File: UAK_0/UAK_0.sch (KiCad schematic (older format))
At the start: 54 parts, among them K1 Кнопка_FSMSM, K2 Кнопка_FSMSM, X1 Крепежное_отверстие_М3, X2 Крепежное_отверстие_М3, X3 Крепежное_отверстие_М3, X4 Крепежное_отверстие_М3

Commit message: подготовлена схема UAK_0A
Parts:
- DA1: renamed from DA?; footprint (none) -> N_DD:DIP6
- gave numbers to parts that had none: 8
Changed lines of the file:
@@
 СДВОЕННЫЙ
 $Comp
-L elements:Предохранитель FU?
+L elements:Предохранитель FU2
 U 1 1 5F560616
 P 5350 5600
-AR Path="/5F560616" Ref="FU?"  Part="1"
+AR Path="/5F560616" Ref="FU2"  Part="1"
 AR Path="/5F540B17/5F560616" Ref="FU?"  Part="1"
-F 0 "FU?" H 5350 5750 60  0000 C CNN
+F 0 "FU2" H 5350 5750 60  0000 C CNN
 F 1 "Предохранитель" H 5350 5450 60  0001 C CNN
 F 2 "N_RLC:Предохранитель_SMD_1812" H 5350 5600 60  0001 C CNN
@@
 $EndComp
 $Comp
-L elements_2020:Клеммник_х2_KLS2-300-5.00-02P-2S XT?
+L elements_2020:Клеммник_х2_KLS2-300-5.00-02P-2S XT8
 U 1 1 5F5696D9
 P 5750 7000
-F 0 "XT?" H 5400 7350 60  0000 L CNN
+F 0 "XT8" H 5400 7350 60  0000 L CNN
 F 1 "Клеммник_х2_KLS2-300-5.00-02P-2S" H 5440 6740 60  0001 C CNN
 F 2 "N_X:Клеммник_х2_шаг5" H 5175 7275 60  0001 C CNN
@@
 220_L
 $Comp
-L elements_2020:МОП-реле_КР293КП1Б DA?
+L elements_2020:МОП-реле_КР293КП1Б DA1
 U 1 1 5F56E7B1
 P 4100 5900
-F 0 "DA?" H 4350 5500 50  0000 C CNN
+F 0 "DA1" H 4350 5500 50  0000 C CNN
 F 1 "МОП-реле_КР293КП1Б" H 4000 6150 50  0001 C CNN
-F 2 "" H 4100 5900 50  0001 C CNN
+F 2 "N_DD:DIP6" H 4100 5900 50  0001 C CNN
 F 3 "" H 4100 5900 50  0001 C CNN
 F 4 "КР293КП1Б/АОУ163А" H 4350 6000 50  0000 C CNN "INFO"
@@
 P 3400 5750
 AR Path="/5F540B17/5F5B8E8E" Ref="R?"  Part="1"
-AR Path="/5F5B8E8E" Ref="R?"  Part="1"
-F 0 "R?" H 3350 5900 60  0000 L CNN
+AR Path="/5F5B8E8E" Ref="R21"  Part="1"
+F 0 "R21" H 3350 5900 60  0000 L CNN
 F 1 "Резистор_0,065Вт" H 3400 5600 60  0001 C CNN
 F 2 "N_RLC:Резистор_SMD_0603_0,065_Вт" H 3400 5750 60  0001 C CNN
@@
 P 3050 7150
 AR Path="/5F540B17/5F5D0ED9" Ref="R?"  Part="1"
-AR Path="/5F5D0ED9" Ref="R?"  Part="1"
-F 0 "R?" H 3000 7000 60  0000 L CNN
+AR Path="/5F5D0ED9" Ref="R20"  Part="1"
+F 0 "R20" H 3000 7000 60  0000 L CNN
 F 1 "Резистор_0,065Вт" H 3050 7000 60  0001 C CNN
 F 2 "N_RLC:Резистор_SMD_0603_0,065_Вт" H 3050 7150 60  0001 C CNN
@@
 P 1950 6650
 AR Path="/5F540B17/5F5D0EE5" Ref="R?"  Part="1"
-AR Path="/5F5D0EE5" Ref="R?"  Part="1"
-F 0 "R?" H 1900 6800 60  0000 L CNN
+AR Path="/5F5D0EE5" Ref="R19"  Part="1"
+F 0 "R19" H 1900 6800 60  0000 L CNN
 F 1 "Резистор_0,065Вт" H 1950 6500 60  0001 C CNN
 F 2 "N_RLC:Резистор_SMD_0603_0,065_Вт" H 1950 6650 60  0001 C CNN
@@
 $EndComp
 $Comp
-L elements_2020:Транзистор_полевой_N-канальный_IRLML6344TR VT?
+L elements_2020:Транзистор_полевой_N-канальный_IRLML6344TR VT4
 U 1 1 5F5D0EF1
 P 3000 6650
-F 0 "VT?" H 3350 7150 60  0000 C CNN
+F 0 "VT4" H 3350 7150 60  0000 C CNN
 F 1 "Транзистор_полевой_N-канальный_IRLML6344TR" H 3200 6400 60  0001 C CNN
 F 2 "MOTOR_VD_VT_HL:Корпус_КТ-46" H 3075 7325 60  0001 C CNN
@@
 	1000 2350 1500 2350
 $Comp
-L elements:Резистор_0,25Вт R?
+L elements:Резистор_0,25Вт R22
 U 1 1 5F6B16D8
 P 4750 6800
-F 0 "R?" V 4705 6903 60  0000 L CNN
+F 0 "R22" V 4705 6903 60  0000 L CNN
 F 1 "Резистор_0,25Вт" H 4750 6650 60  0001 C CNN
 F 2 "N_RLC:Резистор_SMD_1206-0,25_Вт" H 4750 6800 60  0001 C CNN
@@
 КОММУТАЦИЯ 220В
 $Comp
-L elements:Конденсатор_керамический C?
+L elements:Конденсатор_керамический C17
 U 1 1 5F6EF61F
 P 4750 7400
-AR Path="/5F6EF61F" Ref="C?"  Part="1"
+AR Path="/5F6EF61F" Ref="C17"  Part="1"
 AR Path="/5F540B17/5F6EF61F" Ref="C?"  Part="1"
-F 0 "C?" V 4730 7488 60  0000 L CNN
+F 0 "C17" V 4730 7488 60  0000 L CNN
 F 1 "Конденсатор_керамический" H 4850 7300 60  0001 C CNN
 F 2 "N_RLC:Конденсатор_SMD_1210" H 4750 7400 60  0001 C CNN

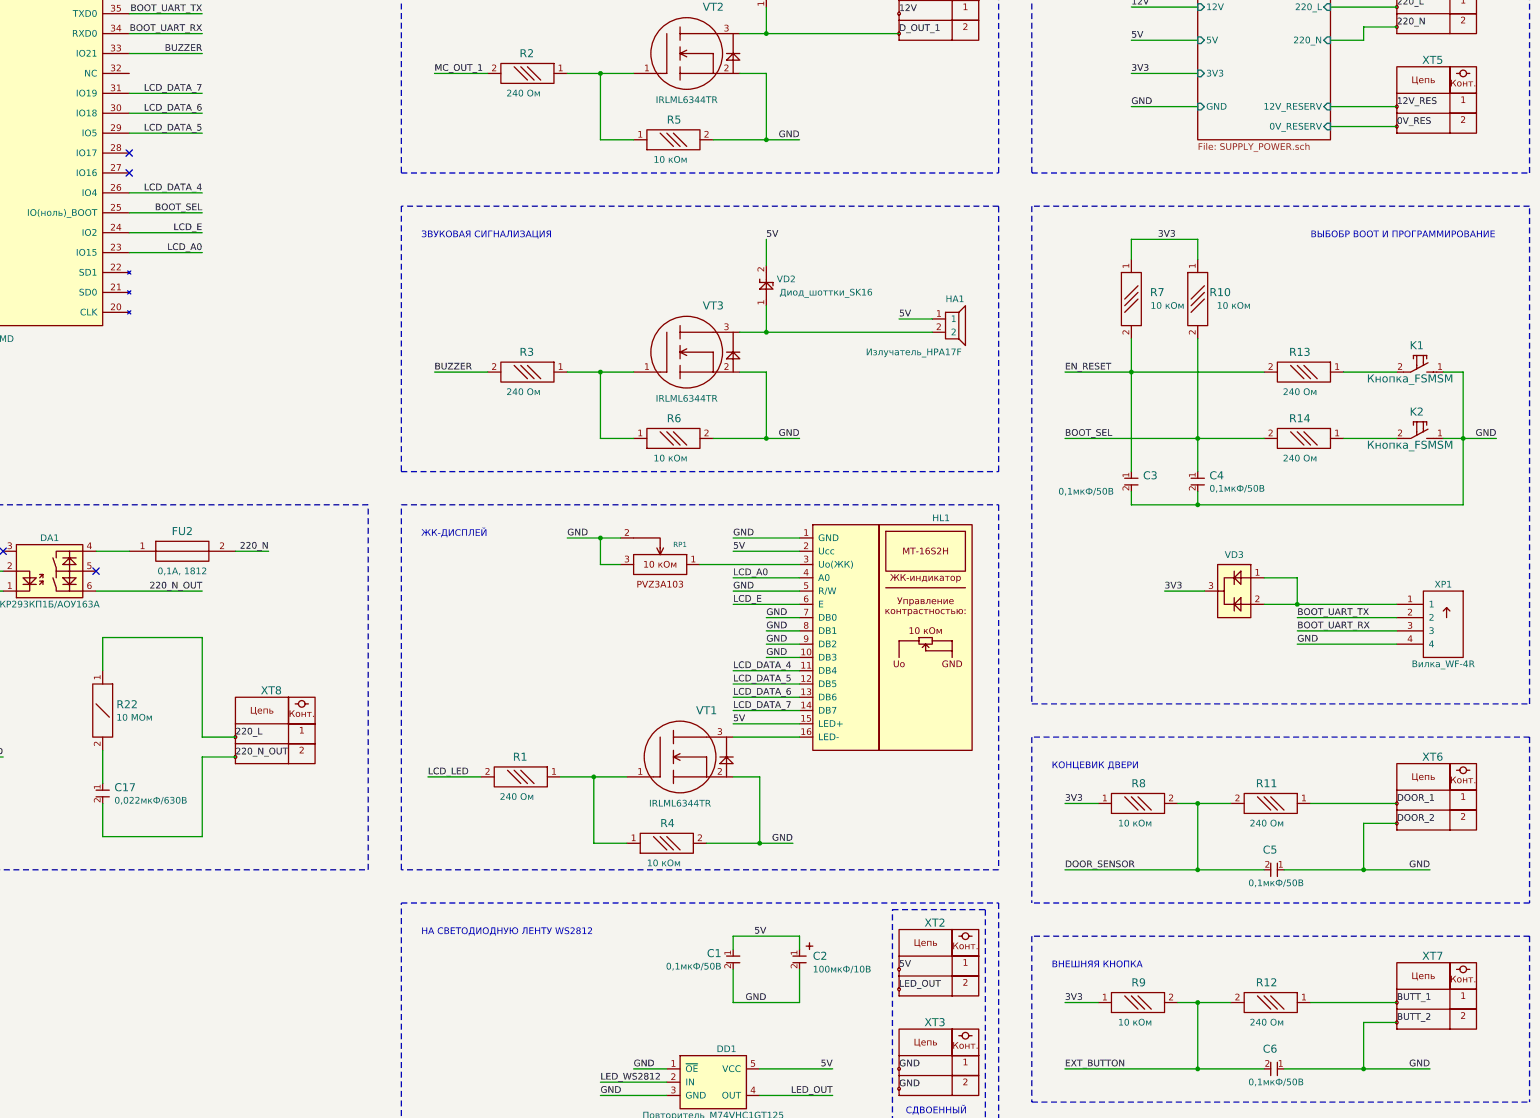
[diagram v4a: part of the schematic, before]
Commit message: есть трассировка питания
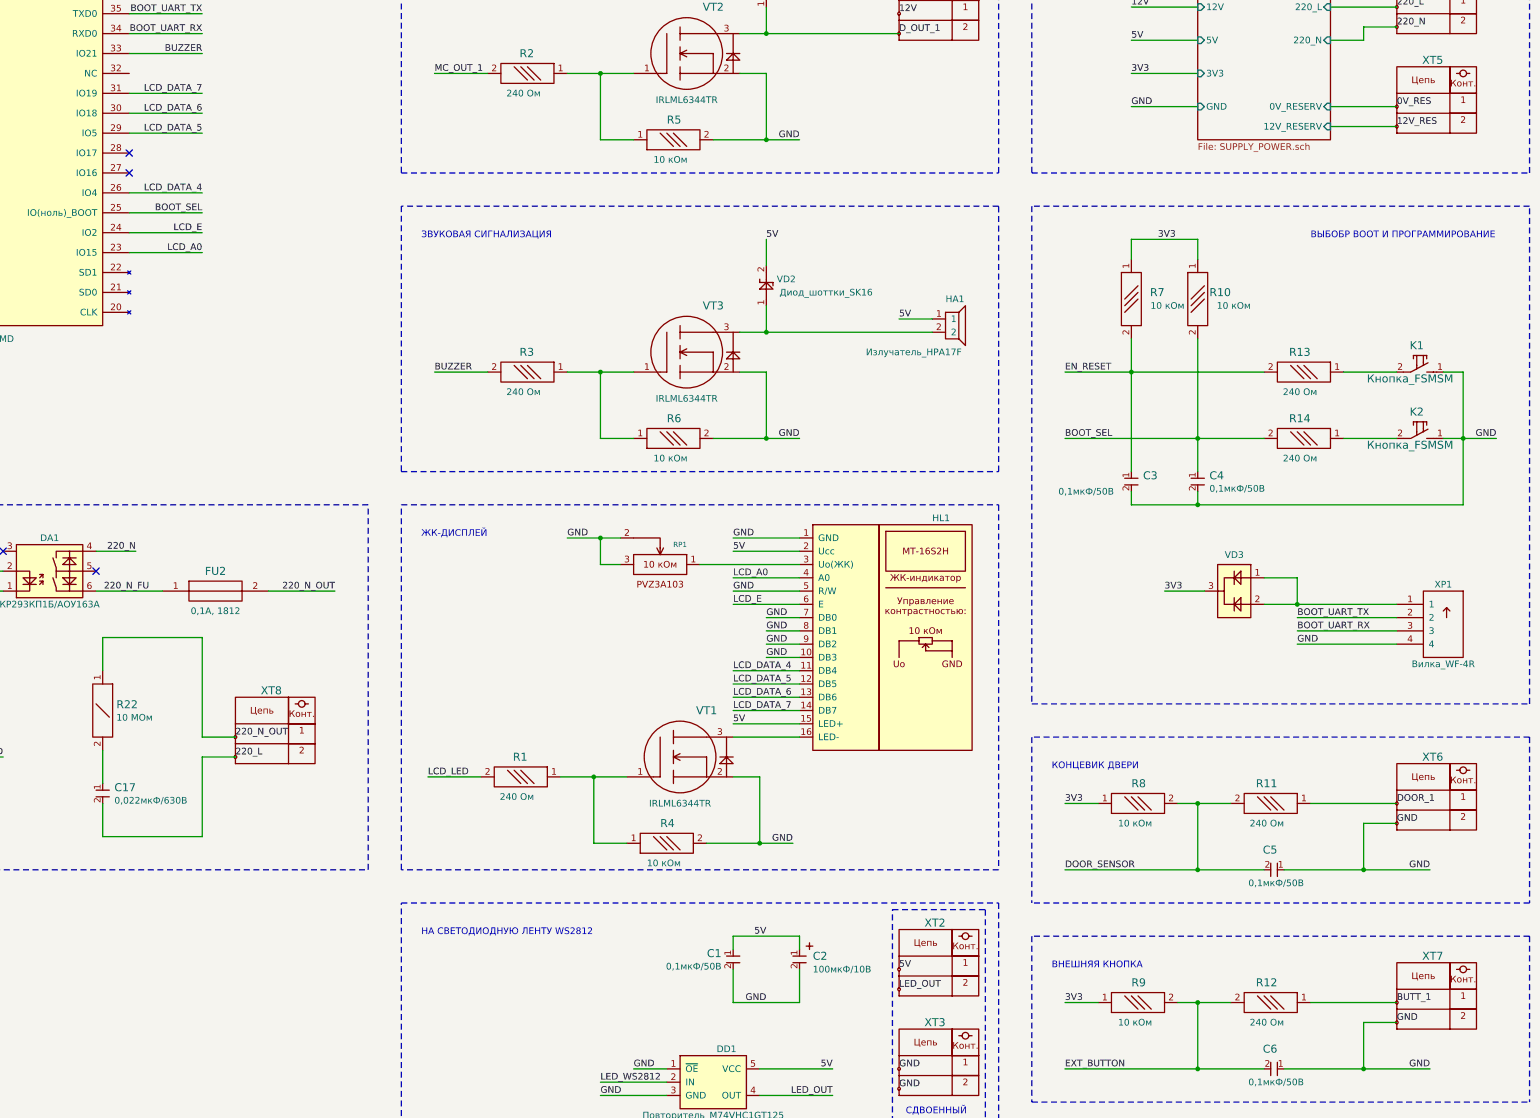
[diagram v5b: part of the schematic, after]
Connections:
- net 0V_RES: now also XT5.1; no longer XT5.2
- net 12V_RES: now also XT5.2; no longer XT5.1
- net 220_L: now also C17.2, XT8.2; no longer R22.1, XT8.1
- net 220_N: now also DA1.4; no longer FU2.2
- net 220_N_OUT: now also FU2.2, R22.1, XT8.1; no longer C17.2, DA1.6, XT8.2
- net 220_N_FU: now reaches FU2.1
- net 220_N_FU: now also DA1.6; no longer DA1.4
- net BUTT_2 renamed GND
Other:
- moved on the sheet: FU2
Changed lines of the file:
@@
 F6 "5V" I L 13000 1750 50
 F7 "12V" I L 13000 1500 50
-F8 "12V_RESERV" I R 14000 2250 50
-F9 "0V_RESERV" I R 14000 2400 50
+F8 "12V_RESERV" I R 14000 2400 50
+F9 "0V_RESERV" I R 14000 2250 50
 $EndSheet
 Wire Wire Line
@@
 Text Label 14500 7500 0    50   ~ 0
 DOOR_1
-Text Label 14500 7650 0    50   ~ 0
-DOOR_2
 Wire Notes Line
 	15500 7000 11750 7000
@@
 Text Label 14500 9000 0    50   ~ 0
 BUTT_1
-Text Label 14500 9150 0    50   ~ 0
-BUTT_2
 Wire Notes Line
 	11750 9750 15500 9750
@@
 Wire Wire Line
 	14000 2400 14500 2400
+Text Label 14500 2400 0    50   ~ 0
+12V_RES
 Text Label 14500 2250 0    50   ~ 0
-12V_RES
-Text Label 14500 2400 0    50   ~ 0
 0V_RES
 Wire Notes Line
@@
 L elements:Предохранитель FU2
 U 1 1 5F560616
-P 5350 5600
+P 5600 5900
 AR Path="/5F560616" Ref="FU2"  Part="1"
 AR Path="/5F540B17/5F560616" Ref="FU?"  Part="1"
-F 0 "FU2" H 5350 5750 60  0000 C CNN
-F 1 "Предохранитель" H 5350 5450 60  0001 C CNN
-F 2 "N_RLC:Предохранитель_SMD_1812" H 5350 5600 60  0001 C CNN
-F 3 "" H 5350 5600 60  0001 C CNN
-F 4 "0,1А, 1812" H 5350 5450 50  0000 C CNN "INFO"
-F 5 "https://www.chipdip.ru/product/mf-msmf010" H 5350 5600 50  0001 C CNN "LINK"
-	1    5350 5600
+F 0 "FU2" H 5600 6050 60  0000 C CNN
+F 1 "Предохранитель" H 5600 5750 60  0001 C CNN
+F 2 "N_RLC:Предохранитель_SMD_1812" H 5600 5900 60  0001 C CNN
+F 3 "" H 5600 5900 60  0001 C CNN
+F 4 "0,1А, 1812" H 5600 5750 50  0000 C CNN "INFO"
+F 5 "https://www.chipdip.ru/product/mf-msmf010" H 5600 5900 50  0001 C CNN "LINK"
+	1    5600 5900
 	1    0    0    -1
 $EndComp
@@
 	-1   0    0    -1
 $EndComp
-Text Label 5750 7000 0    50   ~ 0
+Text Label 5750 7150 0    50   ~ 0
 220_L
 $Comp
@@
 	1    0    0    1
 $EndComp
-Text Label 6000 5600 2    50   ~ 0
+Text Label 5000 5600 2    50   ~ 0
 220_N
-Wire Wire Line
-	6000 5600 5750 5600
 NoConn ~ 4700 5750
 NoConn ~ 4000 5600
-Wire Wire Line
-	4700 5900 5500 5900
-Text Label 5500 5900 2    50   ~ 0
+Text Label 6500 5900 2    50   ~ 0
 220_N_OUT
-Text Label 5750 7150 0    50   ~ 0
+Text Label 5750 7000 0    50   ~ 0
 220_N_OUT
 $Comp
@@
 Wire Wire Line
 	3750 5900 3750 6350
-Wire Wire Line
-	4700 5600 4950 5600
 Text Label 1000 2350 0    50   ~ 0
 MC_220_OUT
@@
 Text Label 2950 5750 0    50   ~ 0
 3V3
+Wire Wire Line
+	4700 5600 5000 5600
+Wire Wire Line
+	6000 5900 6500 5900
+Text Label 5100 5900 2    50   ~ 0
+220_N_FU
+Wire Wire Line
+	4700 5900 5200 5900
+Text Label 14500 7650 0    50   ~ 0
+GND
+Text Label 14500 9150 0    50   ~ 0
+GND
 $EndSCHEMATC

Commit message: начата установка ESP32
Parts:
- C2: symbol MOTOR_2020_components:Конденсатор_К53-56А-32В-22_мкФ+-10проц. -> UAK_0-rescue:Конденсатор_К53-56А-32В-22_мкФ+-10проц.-MOTOR_2020_components
- DA1: symbol elements_2020:МОП-реле_КР293КП1Б -> UAK_0-rescue:МОП-реле_КР293КП1Б-elements_2020
- DD1: symbol elements_2020:Повторитель_M74VHC1GT125 -> UAK_0-rescue:Повторитель_M74VHC1GT125-elements_2020
- HA1: symbol elements_2020:Излучатель_HPA17F -> UAK_0-rescue:Излучатель_HPA17F-elements_2020
- HL1: symbol elements_2020:Жидкокристалический_индикатор_MT-16S2H-2KLW -> UAK_0-rescue:Жидкокристалический_индикатор_MT-16S2H-2KLW-elements_2020
- RP1: symbol elements_2020:Резистор_подстроечный_PVA3A103 -> UAK_0-rescue:Резистор_подстроечный_PVA3A103-elements_2020
- VD1, VD2: symbol elements_2020:Диод_шоттки_SK16 -> UAK_0-rescue:Диод_шоттки_SK16-elements_2020
- VD3: symbol MOTOR_2020_components:Набор_диодов_2Д803АС9 -> UAK_0-rescue:Набор_диодов_2Д803АС9-MOTOR_2020_components
- VT1, VT2, VT3, VT4: symbol elements_2020:Транзистор_полевой_N-канальный_IRLML6344TR -> UAK_0-rescue:Транзистор_полевой_N-канальный_IRLML6344TR-elements_2020
- X1, X2, X3, X4: symbol MOTOR_2020_components:Крепежное_отверстие_М3 -> UAK_0-rescue:Крепежное_отверстие_М3-MOTOR_2020_components
- XP1: symbol MOTOR_2020_components:Вилка_СНП389-4ВП32-1-1 -> UAK_0-rescue:Вилка_СНП389-4ВП32-1-1-MOTOR_2020_components
- XT1, XT2, XT3, XT4, XT5, XT6, XT7, XT8: symbol elements_2020:Клеммник_х2_KLS2-300-5.00-02P-2S -> UAK_0-rescue:Клеммник_х2_KLS2-300-5.00-02P-2S-elements_2020
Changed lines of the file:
@@
 EESchema Schematic File Version 4
 LIBS:UAK_0-cache
-EELAYER 30 0
+EELAYER 29 0
 EELAYER END
 $Descr A3 16535 11693
@@
 $EndComp
 $Comp
-L elements_2020:Клеммник_х2_KLS2-300-5.00-02P-2S XT4
+L UAK_0-rescue:Клеммник_х2_KLS2-300-5.00-02P-2S-elements_2020 XT4
 U 1 1 5F53E542
 P 14500 1500
@@
 	14500 4750 14100 4750
 $Comp
-L MOTOR_2020_components:Набор_диодов_2Д803АС9 VD3
+L UAK_0-rescue:Набор_диодов_2Д803АС9-MOTOR_2020_components VD3
 U 1 1 5F55ECC5
 P 13500 5800
@@
 BOOT_UART_RX
 $Comp
-L MOTOR_2020_components:Вилка_СНП389-4ВП32-1-1 XP1
+L UAK_0-rescue:Вилка_СНП389-4ВП32-1-1-MOTOR_2020_components XP1
 U 1 1 5F5606D4
 P 15000 5900
@@
 	13000 8000 13000 7500
 $Comp
-L elements_2020:Клеммник_х2_KLS2-300-5.00-02P-2S XT6
+L UAK_0-rescue:Клеммник_х2_KLS2-300-5.00-02P-2S-elements_2020 XT6
 U 1 1 5F598429
 P 14500 7500
@@
 КОНЦЕВИК ДВЕРИ
 $Comp
-L elements_2020:Транзистор_полевой_N-канальный_IRLML6344TR VT2
+L UAK_0-rescue:Транзистор_полевой_N-канальный_IRLML6344TR-elements_2020 VT2
 U 1 1 5F5AB6F0
 P 9000 2000
@@
 GND
 $Comp
-L elements_2020:Клеммник_х2_KLS2-300-5.00-02P-2S XT1
+L UAK_0-rescue:Клеммник_х2_KLS2-300-5.00-02P-2S-elements_2020 XT1
 U 1 1 5F5B9CF4
 P 10750 1550
@@
 12V
 $Comp
-L elements_2020:Диод_шоттки_SK16 VD1
+L UAK_0-rescue:Диод_шоттки_SK16-elements_2020 VD1
 U 1 1 5F5C4406
 P 9750 1500
@@
 	4950 2150 5500 2150
 $Comp
-L MOTOR_2020_components:Крепежное_отверстие_М3 X4
+L UAK_0-rescue:Крепежное_отверстие_М3-MOTOR_2020_components X4
 U 1 1 5F5D023C
 P 11000 10500
@@
 $EndComp
 $Comp
-L MOTOR_2020_components:Крепежное_отверстие_М3 X3
+L UAK_0-rescue:Крепежное_отверстие_М3-MOTOR_2020_components X3
 U 1 1 5F5D0231
 P 10500 10500
@@
 $EndComp
 $Comp
-L MOTOR_2020_components:Крепежное_отверстие_М3 X2
+L UAK_0-rescue:Крепежное_отверстие_М3-MOTOR_2020_components X2
 U 1 1 5F5CFEAE
 P 10000 10500
@@
 $EndComp
 $Comp
-L MOTOR_2020_components:Крепежное_отверстие_М3 X1
+L UAK_0-rescue:Крепежное_отверстие_М3-MOTOR_2020_components X1
 U 1 1 5F5CFB44
 P 9500 10500
@@
 	10000 5700 9250 5700
 $Comp
-L elements_2020:Резистор_подстроечный_PVA3A103 RP1
+L UAK_0-rescue:Резистор_подстроечный_PVA3A103-elements_2020 RP1
 U 1 1 5F651E48
 P 9300 5100
@@
 $EndComp
 $Comp
-L elements_2020:Транзистор_полевой_N-канальный_IRLML6344TR VT1
+L UAK_0-rescue:Транзистор_полевой_N-канальный_IRLML6344TR-elements_2020 VT1
 U 1 1 5F61B72E
 P 8950 7300
@@
 	9750 3950 11000 3950
 $Comp
-L elements_2020:Излучатель_HPA17F HA1
+L UAK_0-rescue:Излучатель_HPA17F-elements_2020 HA1
 U 1 1 5F5EFC61
 P 11100 3850
@@
 	9550 3950 9750 3950
 $Comp
-L elements_2020:Диод_шоттки_SK16 VD2
+L UAK_0-rescue:Диод_шоттки_SK16-elements_2020 VD2
 U 1 1 5F5E6E89
 P 9750 3750
@@
 $EndComp
 $Comp
-L elements_2020:Транзистор_полевой_N-канальный_IRLML6344TR VT3
+L UAK_0-rescue:Транзистор_полевой_N-канальный_IRLML6344TR-elements_2020 VT3
 U 1 1 5F5E6E4B
 P 9000 4250
@@
 $EndComp
 $Comp
-L elements_2020:Жидкокристалический_индикатор_MT-16S2H-2KLW HL1
+L UAK_0-rescue:Жидкокристалический_индикатор_MT-16S2H-2KLW-elements_2020 HL1
 U 1 1 5F5D943F
 P 10000 5500
@@
 	13000 9500 13000 9000
 $Comp
-L elements_2020:Клеммник_х2_KLS2-300-5.00-02P-2S XT7
+L UAK_0-rescue:Клеммник_х2_KLS2-300-5.00-02P-2S-elements_2020 XT7
 U 1 1 5F5BFDD6
 P 14500 9000
@@
 NoConn ~ 1500 3400
 $Comp
-L elements_2020:Повторитель_M74VHC1GT125 DD1
+L UAK_0-rescue:Повторитель_M74VHC1GT125-elements_2020 DD1
 U 1 1 5F73F35E
 P 9100 9500
@@
 5V
 $Comp
-L MOTOR_2020_components:Конденсатор_К53-56А-32В-22_мкФ+-10проц. C2
+L UAK_0-rescue:Конденсатор_К53-56А-32В-22_мкФ+-10проц.-MOTOR_2020_components C2
 U 1 1 5F75AF76
 P 10000 8650
@@
 	4950 1400 5500 1400
 $Comp
-L elements_2020:Клеммник_х2_KLS2-300-5.00-02P-2S XT2
+L UAK_0-rescue:Клеммник_х2_KLS2-300-5.00-02P-2S-elements_2020 XT2
 U 1 1 5F79F40F
 P 10750 8750
@@
 $EndComp
 $Comp
-L elements_2020:Клеммник_х2_KLS2-300-5.00-02P-2S XT3
+L UAK_0-rescue:Клеммник_х2_KLS2-300-5.00-02P-2S-elements_2020 XT3
 U 1 1 5F7A0B62
 P 10750 9500
@@
 НА СВЕТОДИОДНУЮ ЛЕНТУ WS2812
 $Comp
-L elements_2020:Клеммник_х2_KLS2-300-5.00-02P-2S XT5
+L UAK_0-rescue:Клеммник_х2_KLS2-300-5.00-02P-2S-elements_2020 XT5
 U 1 1 5F82F0A6
 P 14500 2250
@@
 $EndComp
 $Comp
-L elements_2020:Клеммник_х2_KLS2-300-5.00-02P-2S XT8
+L UAK_0-rescue:Клеммник_х2_KLS2-300-5.00-02P-2S-elements_2020 XT8
 U 1 1 5F5696D9
 P 5750 7000
@@
 220_L
 $Comp
-L elements_2020:МОП-реле_КР293КП1Б DA1
+L UAK_0-rescue:МОП-реле_КР293КП1Б-elements_2020 DA1
 U 1 1 5F56E7B1
 P 4100 5900
@@
 $EndComp
 $Comp
-L elements_2020:Транзистор_полевой_N-канальный_IRLML6344TR VT4
+L UAK_0-rescue:Транзистор_полевой_N-канальный_IRLML6344TR-elements_2020 VT4
 U 1 1 5F5D0EF1
 P 3000 6650

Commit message: закончена трассировка, обновлена PDF и PNG, добавлен STEP
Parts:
- added D1: NI, N_ICO:ni_10x10, symbol elements:LOGO
- added D2: QR, N_ICO:El-nikitos_QR_10x10, symbol elements:LOGO
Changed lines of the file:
@@
 EESchema Schematic File Version 4
 LIBS:UAK_0-cache
-EELAYER 29 0
+EELAYER 30 0
 EELAYER END
 $Descr A3 16535 11693
 encoding utf-8
 Sheet 1 2
-Title ""
+Title "UAK.0B.M9"
 Date ""
 Rev ""
@@
 Text Label 14500 9150 0    50   ~ 0
 GND
+$Comp
+L elements:LOGO D1
+U 1 1 5F67ECD6
+P 8500 10500
+F 0 "D1" H 8425 10700 50  0001 C CNN
+F 1 "NI" H 8450 10500 50  0000 L CNN
+F 2 "N_ICO:ni_10x10" H 8500 10500 50  0001 C CNN
+F 3 "" H 8500 10500 50  0001 C CNN
+	1    8500 10500
+	1    0    0    -1
+$EndComp
+$Comp
+L elements:LOGO D2
+U 1 1 5F67F5F9
+P 9000 10500
+F 0 "D2" H 8925 10700 50  0001 C CNN
+F 1 "QR" H 8950 10500 50  0000 L CNN
+F 2 "N_ICO:El-nikitos_QR_10x10" H 9000 10500 50  0001 C CNN
+F 3 "" H 9000 10500 50  0001 C CNN
+	1    9000 10500
+	1    0    0    -1
+$EndComp
 $EndSCHEMATC

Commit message: UAK_0C. Убрал лого Ni, добавлены gerber
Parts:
- removed D1: NI, N_ICO:ni_10x10, symbol elements:LOGO
- removed D2: QR, N_ICO:El-nikitos_QR_10x10, symbol elements:LOGO
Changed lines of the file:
@@
 EESchema Schematic File Version 4
 LIBS:UAK_0-cache
-EELAYER 30 0
+EELAYER 29 0
 EELAYER END
 $Descr A3 16535 11693
 encoding utf-8
 Sheet 1 2
-Title "UAK.0B.M9"
+Title "UAK.0C.M9"
 Date ""
 Rev ""
@@
 Text Label 14500 9150 0    50   ~ 0
 GND
-$Comp
-L elements:LOGO D1
-U 1 1 5F67ECD6
-P 8500 10500
-F 0 "D1" H 8425 10700 50  0001 C CNN
-F 1 "NI" H 8450 10500 50  0000 L CNN
-F 2 "N_ICO:ni_10x10" H 8500 10500 50  0001 C CNN
-F 3 "" H 8500 10500 50  0001 C CNN
-	1    8500 10500
-	1    0    0    -1
-$EndComp
-$Comp
-L elements:LOGO D2
-U 1 1 5F67F5F9
-P 9000 10500
-F 0 "D2" H 8925 10700 50  0001 C CNN
-F 1 "QR" H 8950 10500 50  0000 L CNN
-F 2 "N_ICO:El-nikitos_QR_10x10" H 9000 10500 50  0001 C CNN
-F 3 "" H 9000 10500 50  0001 C CNN
-	1    9000 10500
-	1    0    0    -1
-$EndComp
 $EndSCHEMATC
